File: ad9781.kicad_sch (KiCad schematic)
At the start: 20 parts, among them J1201 142-0701-201, J1202 142-0701-201, U1201 AD9781BCPZ

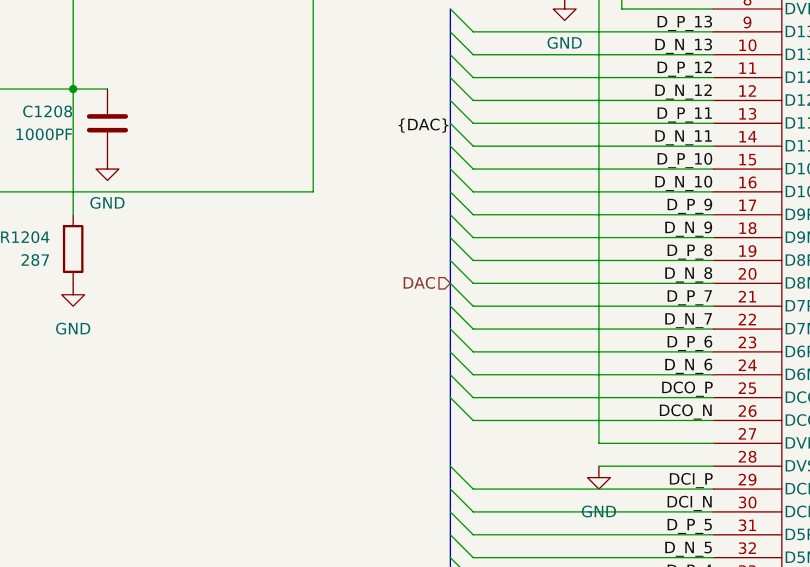
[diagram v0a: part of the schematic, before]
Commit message: Updates from Michal to fix ERC errors
Still lots of ERC warnings
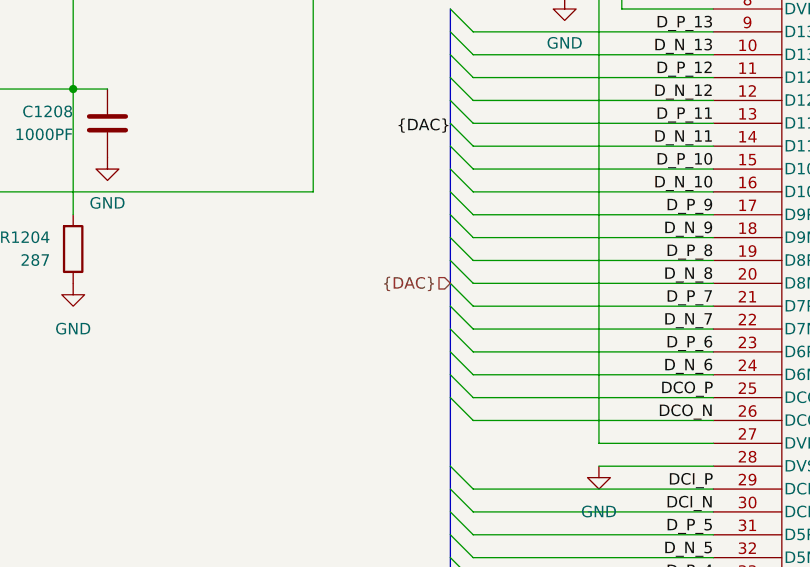
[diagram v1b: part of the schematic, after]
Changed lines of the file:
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@@
 		)
 	)
-	(hierarchical_label "DAC"
+	(hierarchical_label "{DAC}"
 		(shape input)
 		(at 121.92 111.76 180)

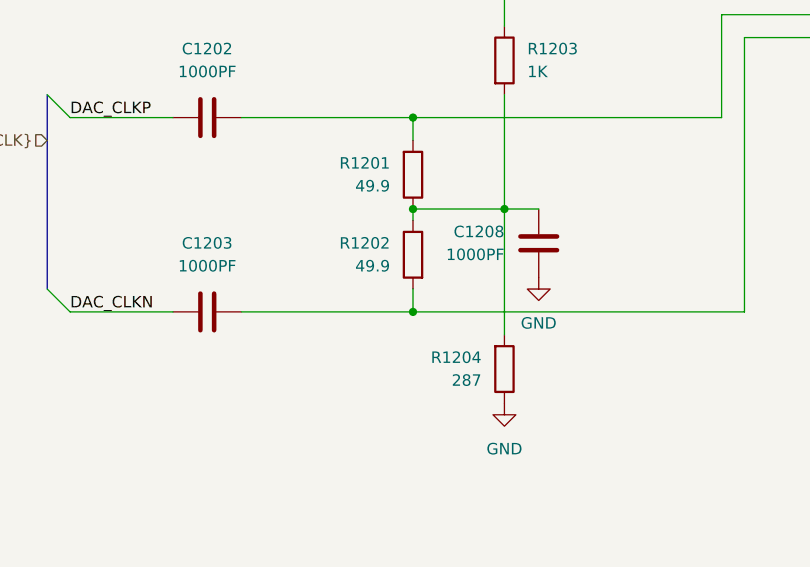
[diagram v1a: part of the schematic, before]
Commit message: Schematic Changes
Added Manufacturer/MPN/Description Fields to parts
Added libraries to project
Modified FMC schematic to use new symbol
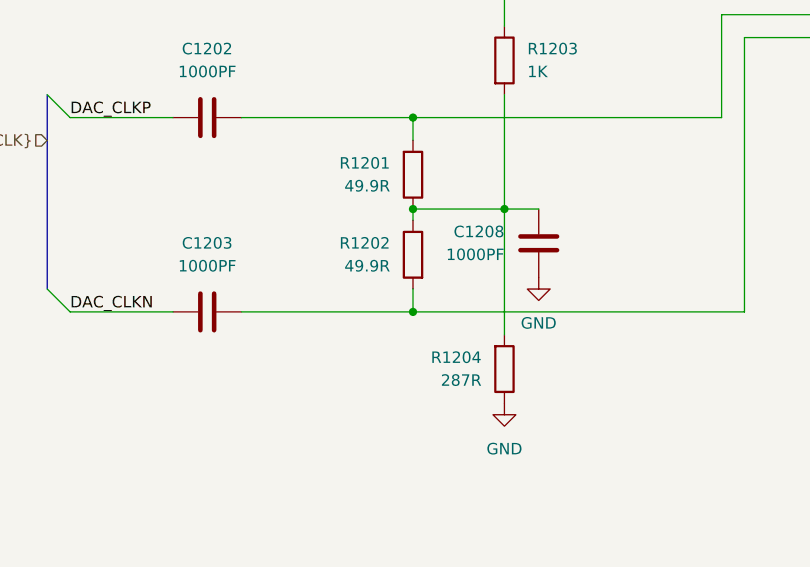
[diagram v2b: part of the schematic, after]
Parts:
- C1201, C1205, C1207, C1210, C1212: Manufacturer (none) -> Murata; Manufacturer Part Number (none) -> GRM155R61A104KA01D
- C1202, C1203, C1208: Manufacturer (none) -> Murata; Manufacturer Part Number (none) -> GRM1885C1H102JA01D
- C1204, C1206, C1209, C1211: Manufacturer (none) -> TDK; Manufacturer Part Number (none) -> C1608X5R1A106M080AC
- J1201, J1202: Manufacturer (none) -> Cinch; Manufacturer Part Number (none) -> 142-0701-201
- R1201, R1202: value 49.9 -> 49.9R; Manufacturer (none) -> YAGEO; Manufacturer Part Number (none) -> RC0603FR-0749R9L
- R1203: Manufacturer (none) -> YAGEO; Manufacturer Part Number (none) -> RC0603FR-071KL
- R1204: value 287 -> 287R; Manufacturer (none) -> YAGEO; Manufacturer Part Number (none) -> RC0603FR-07287RL
- R1205: Manufacturer (none) -> Vishay; Manufacturer Part Number (none) -> MCT0603MD1002DP500
- U1201: Manufacturer (none) -> Analog Devices; Manufacturer Part Number (none) -> AD9781BCPZ

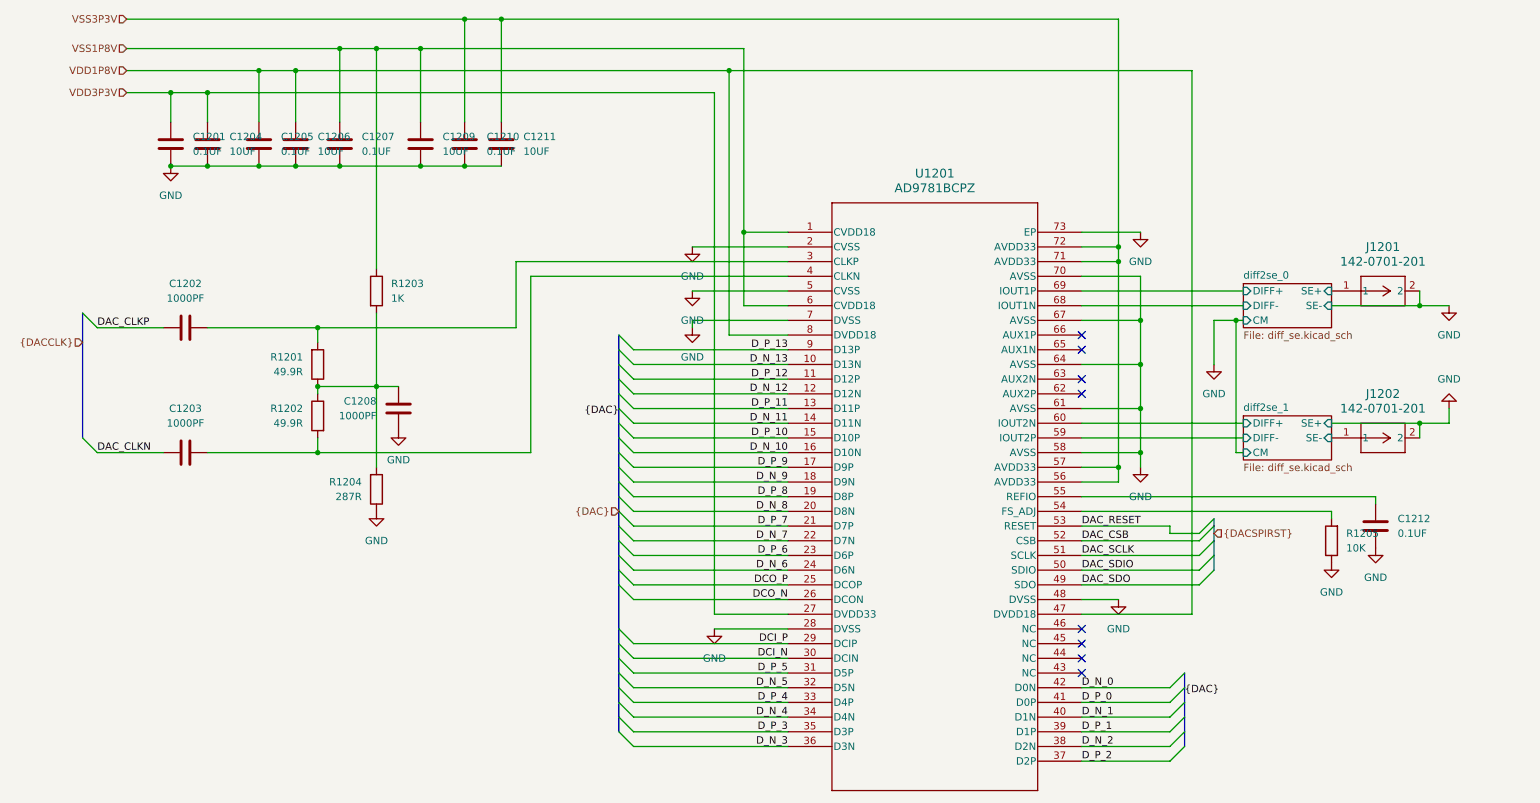
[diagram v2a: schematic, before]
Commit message: Schematics update
Cleaned up RF ADC and front end sections.
Verified that changes did not changes anything about the layout.
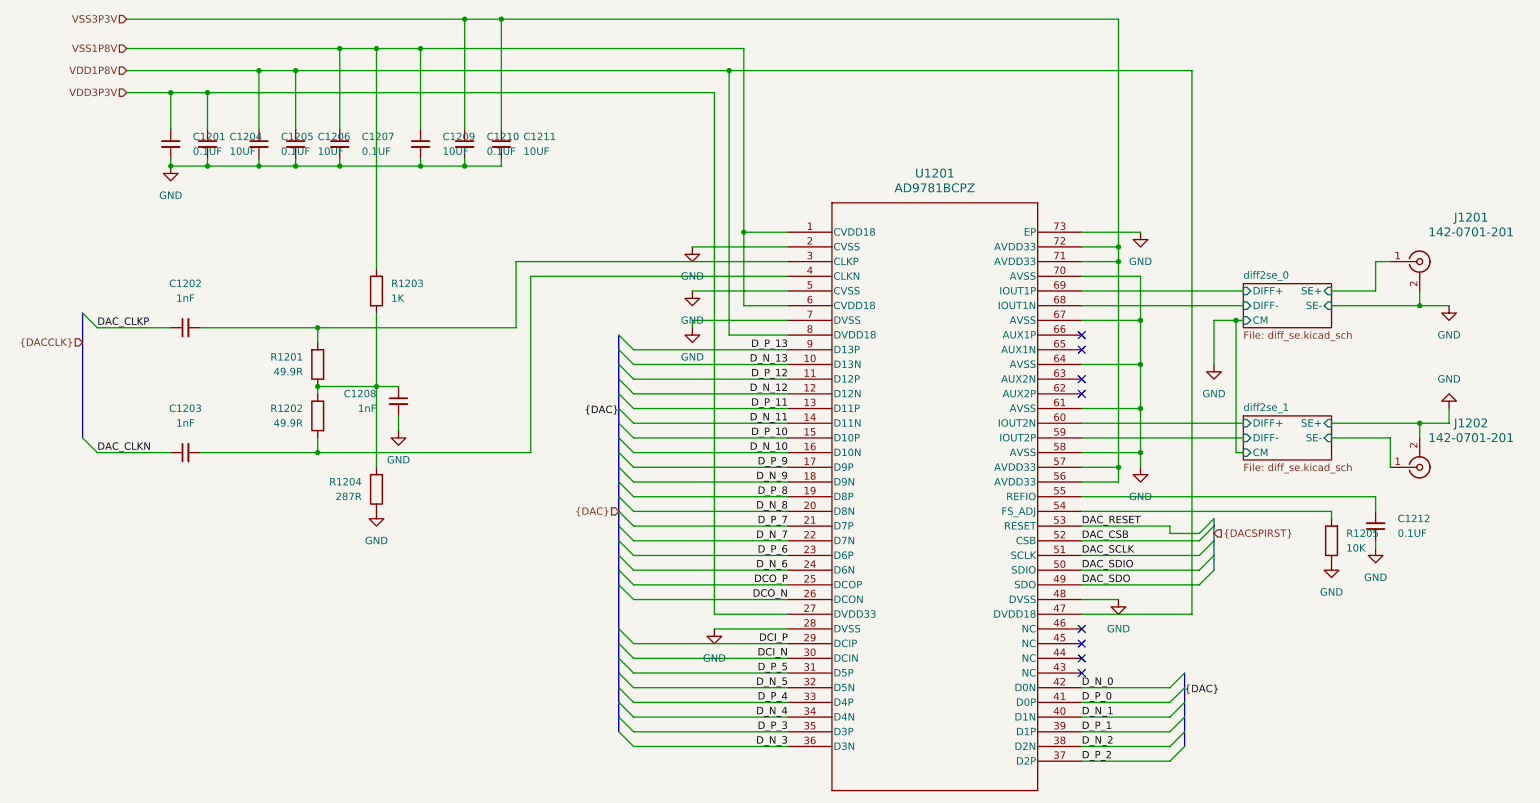
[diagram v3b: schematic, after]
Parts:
- C1201, C1204, C1205, C1206, C1207, C1209, C1210, C1211, C1212: symbol Device:C -> Device:C_Small
- C1202, C1203, C1208: value 1000PF -> 1nF; symbol Device:C -> Device:C_Small
- J1201, J1202: symbol 001_symbol:142-0701-201_GH -> Zest_Custom:SMA_Coaxial
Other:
- moved on the sheet: C1208

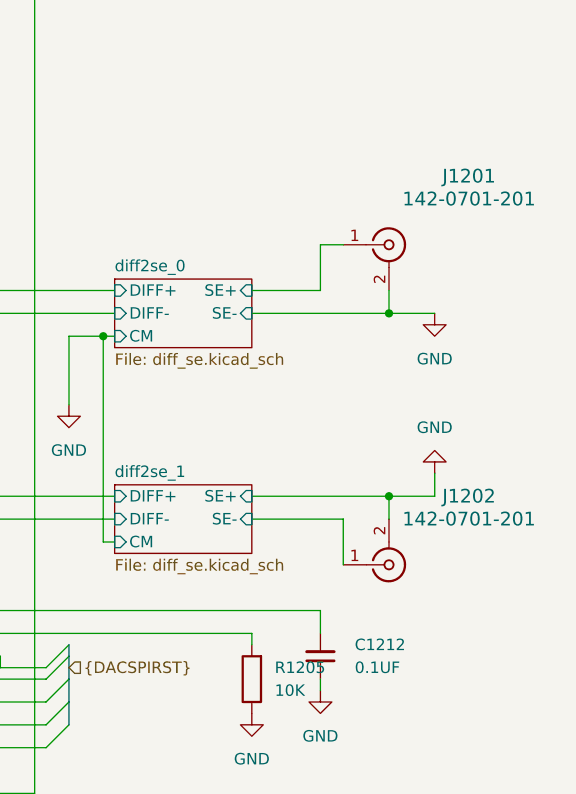
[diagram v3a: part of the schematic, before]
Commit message: Further Project cleanup
-Added BOM and fabrication files
-updated all documentation files
- Added suggested DC blocking cap at DAC outputs

-Set DRC to 5mil trace and space and fixed various violations detailed below
- Removed various small tracks overlapping IC pads on U2701,U2901,U3101,U3201
- Spaced vias 5 mil apart around U701, U201, 1201
- Moved LMK_CLKout3 pair on In4 layer away from PMOD1_1 pin
- adjusted track into pin47 on U701 to clear pin 48
- adjusted trace under U903 to give more room from ground pads/vias
- spaced out vias around pins45/46 of U201

-Many tweak to trace to go through the center of pad throughout the design
-An example is the trace around C3005
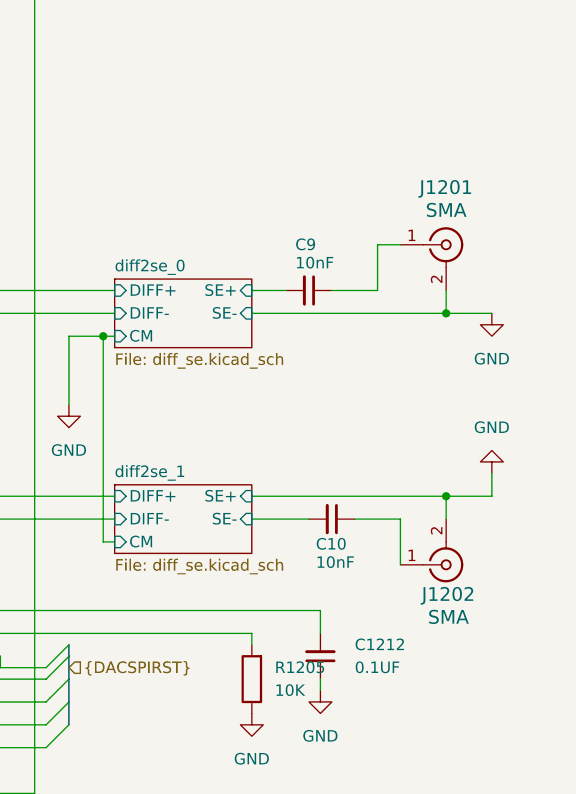
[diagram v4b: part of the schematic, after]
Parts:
- added C10, C9: 10nF, Capacitor_SMD:C_0603_1608Metric, symbol Device:C_Small
- J1201, J1202: value 142-0701-201 -> SMA
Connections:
- net diff2se_0/SE+: now also C9.2; no longer J1201.1 (In)
- net diff2se_1/SE-: now also C10.2; no longer J1202.1 (In)
- new net: C9.1, J1201.1 (In)
- new net: C10.1, J1202.1 (In)
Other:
- moved on the sheet: J1201, J1202

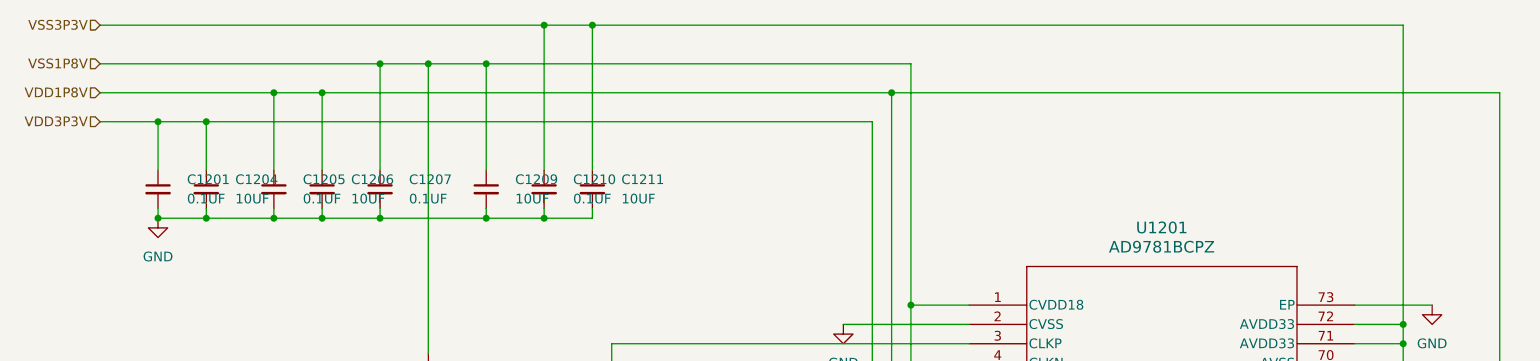
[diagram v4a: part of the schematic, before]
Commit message: Changes to project for Final Review
- Changed R2001 & R2002 to DNP (these are accel. I2C pull ups)
- Added additional 100nF bypass caps to RF DAC on 1.8V and 3.3V rails [C1213,C1214]
- Added ORNL and Osprey Logo to Board
-Added Fab notes to F.Fab layer from the original PADS project
-- Adjusted Board stackup details to match these new notes

-Layout Tweaks/fixes:
- Deleted stray GND via under U1002 that is cutting up LMK2468_plane on In6.Cu
- Enlarged to 20mil LMK57_plane trace on In2.Cu (near U1002) (was12mil)
- Added second via to pin 6 of U1002 to LMK13_plane like others
- Added vias to VSS3P3V trace to connect to planes (starts near U3101)
- Added 4 GND vias under U2701 & U2901 (recommended layout has 6 ; had 1)
- Centered U701 pin 4 trace
- Make U701 traces to pins 45/46 smaller
- adjusted traces near 4 via clusters at U201 pins 45/46 and 3/4 to get rid of sharp corners
- centered U3201 pin 8/10/11 traces like U3101?
- U1201 pin 27, connected 2 VDD3P3V vias with trace on top layer
- U1201 pin 47, connected 3 VDD1P8V vias with trace on top layer
- Got rid of U1201 pin 56/57 via traces sharp corner, and added 2 additional vias like pins 71/72
- U1201: C1211 is 10uF for pins 56/57 and C1210 is 0.1uF for pins 71/72. Changed both to 0.1uF [adding C1213 mentioned eariler] and moved 10uF between the 2 0.1uF caps
- C1704 shown to U1701 pins 23/24 in sch but connected to U1201 pin 8 on PCB, and C201 close to U1701 pins 23/24 on PCB but connected to U201 pins 8/29 in sch (U701 has cap near pin 29 but U201 does not) - moveed caps to match sch and add bypass cap to U1201 DAC chip [C1214 mentioned earlier]

- It might be good to beef up the traces and number of vias to/from R901 and the In6.Cu plane for the VDD3P3V

-Regenerated all fabrication and documentation prints
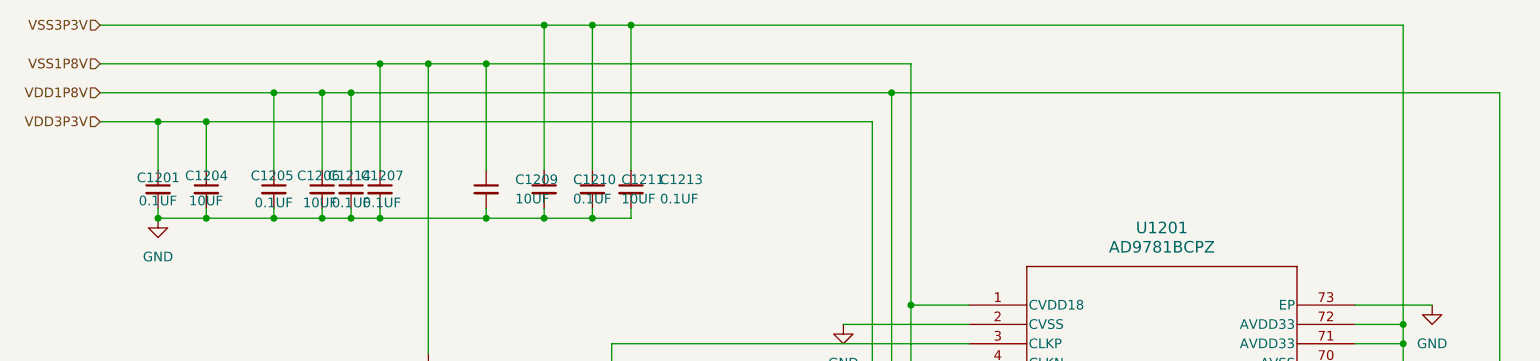
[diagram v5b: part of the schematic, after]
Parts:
- added C1213, C1214: 0.1UF, Capacitor_SMD:C_0402_1005Metric, symbol Device:C_Small
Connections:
- net GND: now also C1213.2, C1214.2
- net VDD1P8V: now also C1214.1
- net VSS3P3V: now also C1213.1
